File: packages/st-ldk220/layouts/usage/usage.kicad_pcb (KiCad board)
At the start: 2 copper layers, 5 parts

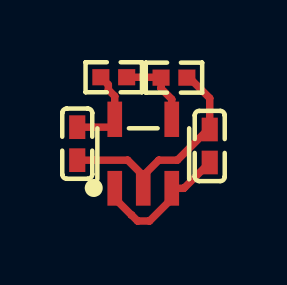
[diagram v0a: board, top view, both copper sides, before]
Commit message: Clean PR: Only include packages from package-todos.md
- Updated layouts and parts for packages listed in package-todos.md only
- Includes adi-ad5693r, adi-adbms6822, adi-adbms6830, adi-adxl375, adi-ltc4316
- Updated ams-tsl2591, aosong-aht20, bosch sensors, diodes-inc, espressif
- Updated infineon, invensense, issi, liteon, macroblock, maxim components
- Updated memsic, microchip, rohm, nxp, opsco, st, ti, usb-connectors
- Renamed pjrc-teensy_4_1 to pjrc-teensy-4-1 (hyphen naming convention)
- Updated realtek-rtl8305nb

Removed 64+ packages that were not listed in package-todos.md to keep
PR focused only on packages that are being tracked for review.
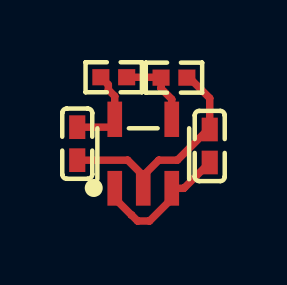
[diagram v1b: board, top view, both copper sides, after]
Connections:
- net ADJ_NC renamed VDIV_OUTPUT
- net EN renamed power_in-VCC
- net gnd renamed GND
- net hv renamed power_shim-VCC
